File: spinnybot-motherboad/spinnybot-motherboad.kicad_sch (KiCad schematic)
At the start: 52 parts, among them J1 LEDSTRIP1_CONN, J10 M2_GND, J11 M3_12V, J12 M3_GND, J13 GND, J14 M2_12V, J15 M3_SERIAL_CONN, J16 M2_SERIAL_CONN, J17 M1_SERIAL_CONN, J2 LEDSTRIP2_CONN, J3 LEDSTRIP3_CONN, J4 XBEE RESET, J5 XBEE FTDI, J6 CAP SWITCH, J7 +12V, J8 M1_12V, J9 M1_GND, Q1 SISA96DN, U1 SN74AHCT541N, U2 LM1117-5.0, U3 LM1117-3.3, U4 SN74LVC1G74, U5 XBP9B-DMWT-002

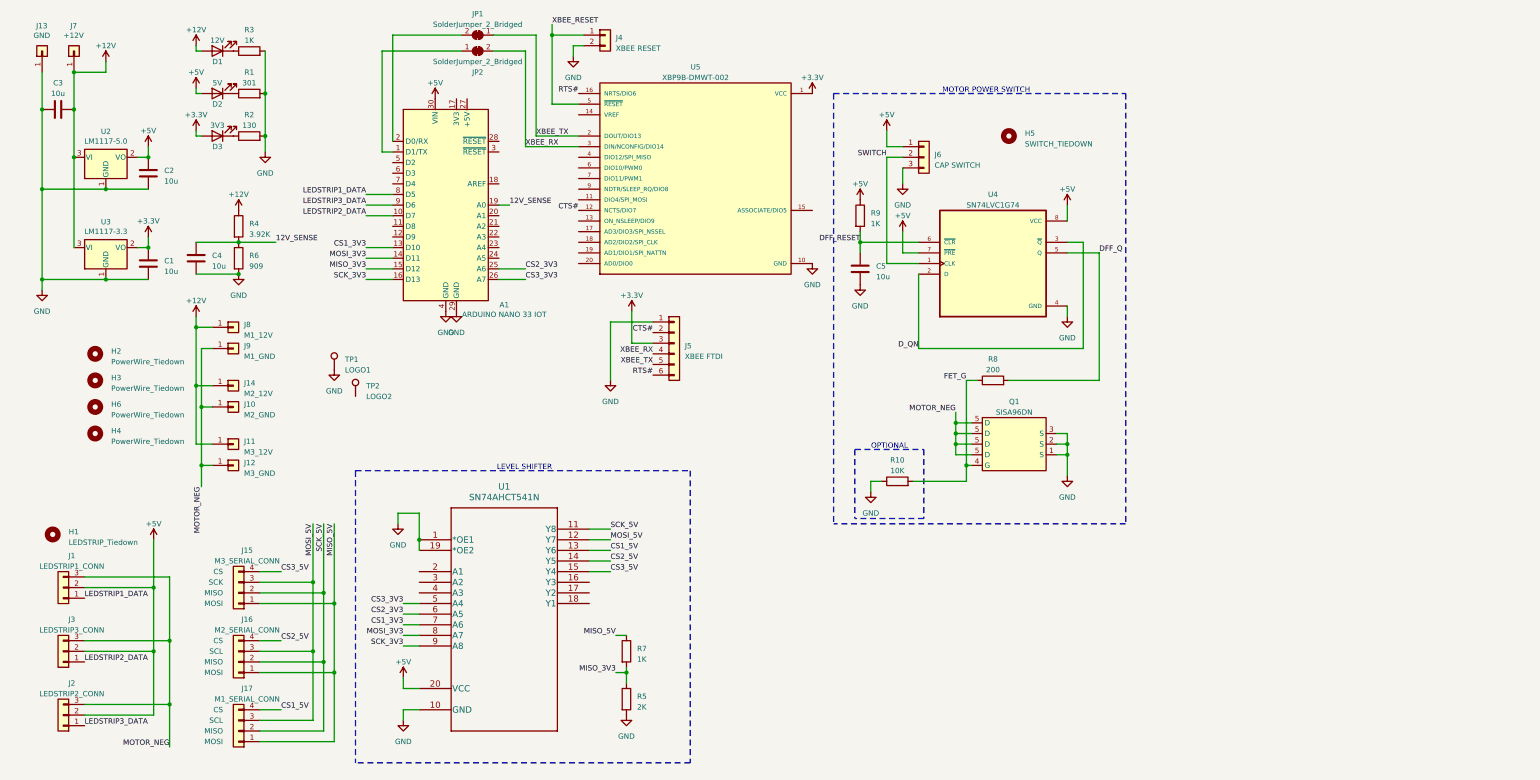
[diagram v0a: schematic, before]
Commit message: board rev 2, got all components placed. still need to route
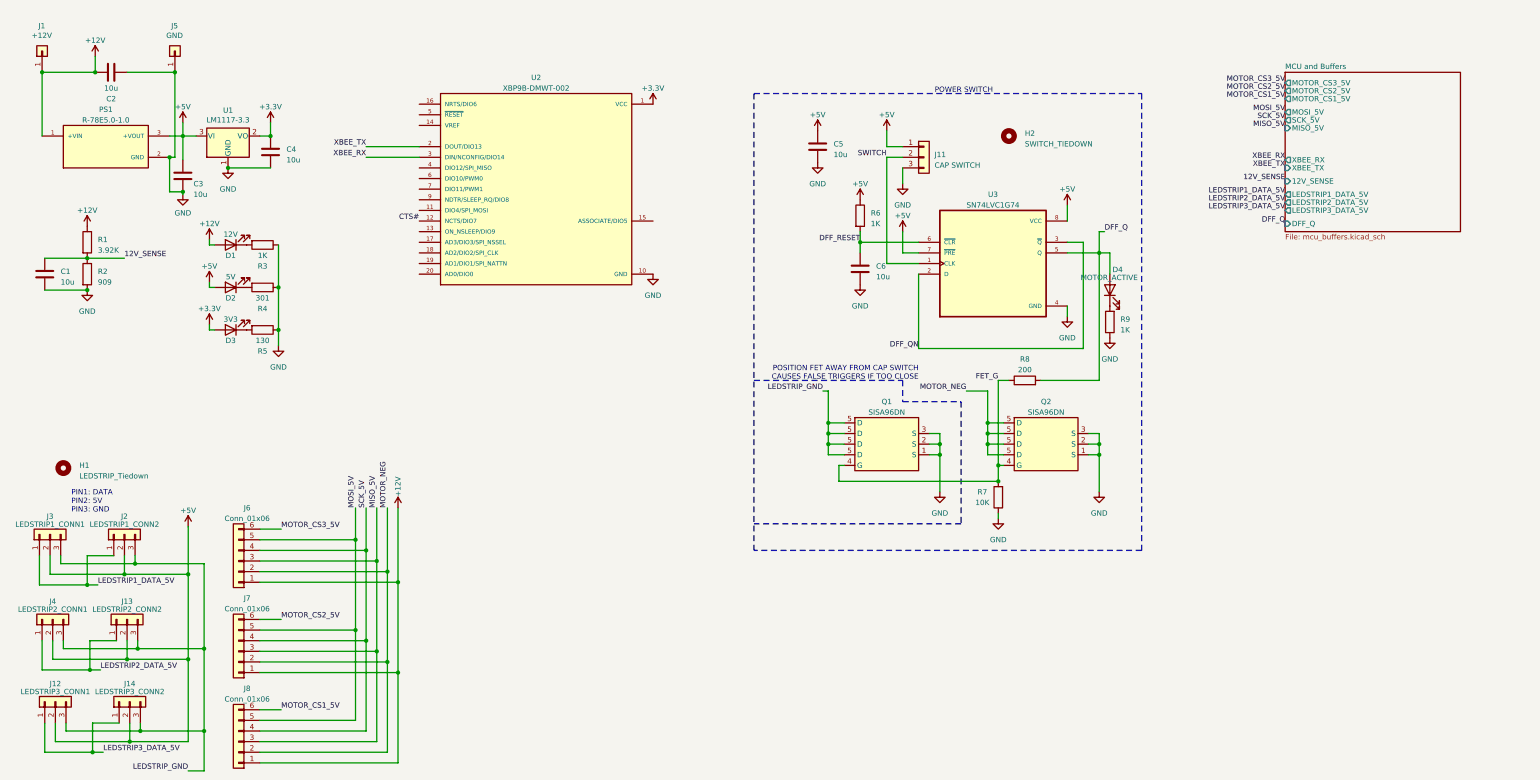
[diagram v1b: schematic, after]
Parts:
- removed A1: ARDUINO NANO 33 IOT, Module:Arduino_Nano, symbol MCU_Module:Arduino_Nano_v3.x
- removed C1, C2: 10u, Capacitor_SMD:C_1206_3216Metric_Pad1.33x1.80mm_HandSolder, symbol Device:C
- removed H2, H3, H4, H6: PowerWire_Tiedown, MountingHole:MountingHole_3mm, symbol Mechanical:MountingHole
- removed J10: M2_GND, TestPoint:TestPoint_Pad_2.5x2.5mm, symbol Connector_Generic:Conn_01x01
- removed J11: M3_12V, TestPoint:TestPoint_Pad_2.5x2.5mm, symbol Connector_Generic:Conn_01x01
- removed J12: M3_GND, TestPoint:TestPoint_Pad_2.5x2.5mm, symbol Connector_Generic:Conn_01x01
- removed J14: M2_12V, TestPoint:TestPoint_Pad_2.5x2.5mm, symbol Connector_Generic:Conn_01x01
- removed J15: M3_SERIAL_CONN, Connector_PinHeader_2.54mm:PinHeader_1x04_P2.54mm_Vertical, symbol spinnybot:motor_serial_connector
- removed J16: M2_SERIAL_CONN, Connector_PinHeader_2.54mm:PinHeader_1x04_P2.54mm_Vertical, symbol spinnybot:motor_serial_connector
- removed J17: M1_SERIAL_CONN, Connector_PinHeader_2.54mm:PinHeader_1x04_P2.54mm_Vertical, symbol spinnybot:motor_serial_connector
- removed J2: LEDSTRIP2_CONN, Connector_PinHeader_2.54mm:PinHeader_1x03_P2.54mm_Vertical, symbol Connector_Generic:Conn_01x03
- removed J4: XBEE RESET, Connector_PinHeader_2.54mm:PinHeader_1x02_P2.54mm_Vertical, symbol Connector_Generic:Conn_01x02
- removed J5: XBEE FTDI, Connector_PinHeader_2.54mm:PinHeader_1x06_P2.54mm_Vertical, symbol Connector_Generic:Conn_01x06
- removed J8: M1_12V, TestPoint:TestPoint_Pad_2.5x2.5mm, symbol Connector_Generic:Conn_01x01
- removed J9: M1_GND, TestPoint:TestPoint_Pad_2.5x2.5mm, symbol Connector_Generic:Conn_01x01
- removed JP1, JP2: SolderJumper_2_Bridged, Jumper:SolderJumper-2_P1.3mm_Open_RoundedPad1.0x1.5mm, symbol Jumper:SolderJumper_2_Bridged
- removed R5: 2K, Resistor_SMD:R_0805_2012Metric_Pad1.20x1.40mm_HandSolder, symbol Device:R
- removed R7: 1K, Resistor_SMD:R_0805_2012Metric_Pad1.20x1.40mm_HandSolder, symbol Device:R
- removed TP1: LOGO1, robologo-shenzen:F.Mask_g1609, symbol Connector:TestPoint
- removed TP2: LOGO2, robologo-shenzen:F.SilkS_g1611, symbol Connector:TestPoint
- removed U1: SN74AHCT541N, SN74AHCT541N:SN74AHCT541N, symbol SN74AHCT541N:SN74AHCT541N
- removed U2: LM1117-5.0, Package_TO_SOT_SMD:SOT-223-3_TabPin2, symbol Regulator_Linear:LM1117-5.0
- removed U3: LM1117-3.3, Package_TO_SOT_SMD:SOT-223-3_TabPin2, symbol Regulator_Linear:LM1117-3.3
- added C3, C4, C5: 10u, Capacitor_SMD:C_1206_3216Metric_Pad1.33x1.80mm_HandSolder, symbol Device:C
- added D4: MOTOR_ACTIVE, LED_SMD:LED_0805_2012Metric_Pad1.15x1.40mm_HandSolder, symbol Device:LED
- added J12: LEDSTRIP3_CONN1, B3B-PH-SM4:JST_B3B-PH-SM4-TB(LF)(SN), symbol Connector_Generic:Conn_01x03
- added J13: LEDSTRIP2_CONN2, B3B-PH-SM4:JST_B3B-PH-SM4-TB(LF)(SN), symbol Connector_Generic:Conn_01x03
- added J14: LEDSTRIP3_CONN2, B3B-PH-SM4:JST_B3B-PH-SM4-TB(LF)(SN), symbol Connector_Generic:Conn_01x03
- added J4: LEDSTRIP2_CONN1, B3B-PH-SM4:JST_B3B-PH-SM4-TB(LF)(SN), symbol Connector_Generic:Conn_01x03
- added J6, J7, J8: Conn_01x06, S6B-XH-SM4-TB:S6B-XH-SM4-TBLFSN, symbol Connector_Generic:Conn_01x06
- added PS1: R-78E5.0-1.0, R-78E5:CONV_R-78E5.0-1.0, symbol R-78E5.0-1.0:R-78E5.0-1.0
- added Q1: SISA96DN, Package_SO:Vishay_PowerPAK_1212-8_Single, symbol spinnybot:SISA96DN
- added R9: 1K, Resistor_SMD:R_0805_2012Metric_Pad1.20x1.40mm_HandSolder, symbol Device:R
- added U1: LM1117-3.3, Package_TO_SOT_SMD:SOT-223-3_TabPin2, symbol Regulator_Linear:LM1117-3.3
- J2: renamed from J1; value LEDSTRIP1_CONN -> LEDSTRIP1_CONN2; footprint Connector_PinHeader_2.54mm:PinHeader_1x03_P2.54mm_Vertical -> B3B-PH-SM4:JST_B3B-PH-SM4-TB(LF)(SN)
- J3: value LEDSTRIP3_CONN -> LEDSTRIP1_CONN1; footprint Connector_PinHeader_2.54mm:PinHeader_1x03_P2.54mm_Vertical -> B3B-PH-SM4:JST_B3B-PH-SM4-TB(LF)(SN)
- renumbered C4 to C1, C3 to C2, C5 to C6, H5 to H2, J7 to J1, J6 to J11, J13 to J5, Q1 to Q2, R4 to R1, R6 to R2, R1 to R4, R2 to R5, R9 to R6, R10 to R7, U5 to U2, U4 to U3
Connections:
- net LEDSTRIP2_DATA is gone; now on net LEDSTRIP1_DATA_5V: J3.1 (Pin_1)
- net +12V: now also J6.1 (Pin_1), J7.1 (Pin_1), J8.1 (Pin_1), PS1.1 (+VIN)
- net +3V3: now also C4.1, U1.2 (VO)
- net +5V: now also C3.1, C5.1, J12.2 (Pin_2), J13.2 (Pin_2), J14.2 (Pin_2), J4.2 (Pin_2), PS1.3 (+VOUT), U1.3 (VI)
- net DFF_Q: now also D4.2 (A)
- net FET_G: now also Q1.4 (G)
- net GND: now also R3.1, R4.1, R5.1, C3.2, C4.2, C5.2, PS1.2 (GND), Q1.1 (S), Q1.2 (S), Q1.3 (S), R9.1, U1.1 (GND); no longer R3.2, R4.2, R5.2
- net MISO_5V: now also J6.3 (Pin_3), J7.3 (Pin_3), J8.3 (Pin_3)
- net MOSI_5V: now also J6.5 (Pin_5), J7.5 (Pin_5), J8.5 (Pin_5)
- net MOTOR_NEG: now also J6.2 (Pin_2), J7.2 (Pin_2), J8.2 (Pin_2); no longer J2.3 (Pin_3), J3.3 (Pin_3)
- net SCK_5V: now also J6.4 (Pin_4), J7.4 (Pin_4), J8.4 (Pin_4)
- net at D3.1 (K): now also R5.2; no longer R5.1
- net at D1.1 (K): now also R3.2; no longer R3.1
- net at D2.1 (K): now also R4.2; no longer R4.1
- net D_QN renamed DFF_QN
- net LEDSTRIP1_DATA renamed LEDSTRIP1_DATA_5V
- net RTS#: no longer names the net of U2.16 (NRTS/DIO6)
- net XBEE_RESET: no longer names the net of U2.5 (~RESET)
- new net: D4.1 (K), R9.2
- new net LEDSTRIP2_DATA_5V: J13.1 (Pin_1), J4.1 (Pin_1)
- new net LEDSTRIP3_DATA_5V: J12.1 (Pin_1), J14.1 (Pin_1)
- new net LEDSTRIP_GND: J12.3 (Pin_3), J13.3 (Pin_3), J14.3 (Pin_3), J2.3 (Pin_3), J3.3 (Pin_3), J4.3 (Pin_3), Q1.5 (D)
- new net MOTOR_CS1_5V: J8.6 (Pin_6)
- new net MOTOR_CS2_5V: J7.6 (Pin_6)
- new net MOTOR_CS3_5V: J6.6 (Pin_6)
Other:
- added sheet MCU and Buffers (mcu_buffers.kicad_sch)
- note added: "PIN1: DATA PIN2: 5V PIN3: GND"
- note added: "POSITION FET AWAY FROM CAP SWITCH CAUSES FALSE TRIGGERS IF TOO CLOSE"
- note added: "POWER SWITCH"
- note removed: "LEVEL SHIFTER"
- note removed: "MOTOR POWER SWITCH"
- note removed: "OPTIONAL"
- moved on the sheet: C1, C2, D1, D2, D3, H1, J1, J2, J5, Q2, R1, R2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

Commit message: routed rev2 mainboard
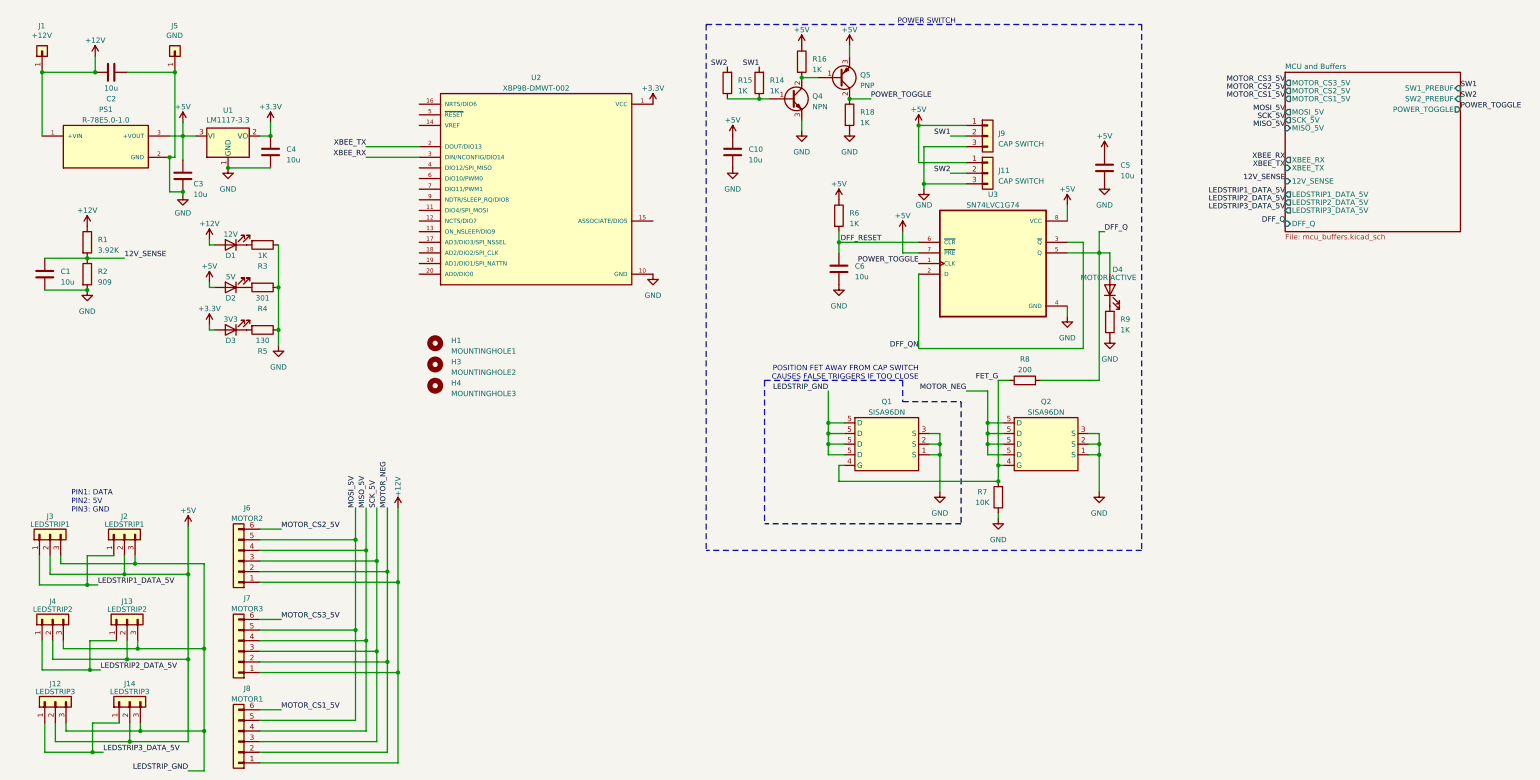
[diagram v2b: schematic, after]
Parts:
- removed H2: SWITCH_TIEDOWN, MountingHole:MountingHole_3mm, symbol Mechanical:MountingHole
- added C10: 10u, Capacitor_SMD:C_1206_3216Metric_Pad1.33x1.80mm_HandSolder, symbol Device:C
- added H3: MOUNTINGHOLE2, custom:MountingHole_3.3mm, symbol Mechanical:MountingHole
- added H4: MOUNTINGHOLE3, custom:MountingHole_3.3mm, symbol Mechanical:MountingHole
- added J9: CAP SWITCH, B3B-PH-SM4:JST_B3B-PH-SM4-TB(LF)(SN), symbol Connector_Generic:Conn_01x03
- added Q4: NPN, Package_TO_SOT_THT:TO-92_Inline, symbol Device:Q_NPN_BCE
- added Q5: PNP, Package_TO_SOT_THT:TO-92_Inline, symbol Device:Q_PNP_BCE
- added R14, R15, R16, R18: 1K, Resistor_SMD:R_0805_2012Metric_Pad1.20x1.40mm_HandSolder, symbol Device:R
- D4: value MOTOR_ACTIVE -> MOTOR ACTIVE
- H1: value LEDSTRIP_Tiedown -> MOUNTINGHOLE1; footprint MountingHole:MountingHole_3mm -> custom:MountingHole_3.3mm
- J11: footprint Connector_PinHeader_2.54mm:PinHeader_1x03_P2.54mm_Vertical -> B3B-PH-SM4:JST_B3B-PH-SM4-TB(LF)(SN)
- J12: value LEDSTRIP3_CONN1 -> LEDSTRIP3
- J13: value LEDSTRIP2_CONN2 -> LEDSTRIP2
- J14: value LEDSTRIP3_CONN2 -> LEDSTRIP3
- J2: value LEDSTRIP1_CONN2 -> LEDSTRIP1
- J3: value LEDSTRIP1_CONN1 -> LEDSTRIP1
- J4: value LEDSTRIP2_CONN1 -> LEDSTRIP2
- J5: footprint Connector_Wire:SolderWirePad_1x01_SMD_5x10mm -> custom:Stitched_SolderWirePad_1x01_SMD_5x10mm
- J6: value Conn_01x06 -> MOTOR2
- J7: value Conn_01x06 -> MOTOR3
- J8: value Conn_01x06 -> MOTOR1
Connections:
- net +5V: now also C10.1, J9.1 (Pin_1), Q5.3 (E), R16.1
- net GND: now also C10.2, J9.3 (Pin_3), Q4.3 (E), R18.2
- net MISO_5V: now also J6.4 (Pin_4), J7.4 (Pin_4), J8.4 (Pin_4); no longer J6.3 (Pin_3), J7.3 (Pin_3), J8.3 (Pin_3)
- net MOTOR_CS2_5V: now also J6.6 (Pin_6); no longer J7.6 (Pin_6)
- net MOTOR_CS3_5V: now also J7.6 (Pin_6); no longer J6.6 (Pin_6)
- net SCK_5V: now also J6.3 (Pin_3), J7.3 (Pin_3), J8.3 (Pin_3); no longer J6.4 (Pin_4), J7.4 (Pin_4), J8.4 (Pin_4)
- net CTS#: no longer names the net of U2.12 (NCTS/DIO7)
- net SWITCH renamed POWER_TOGGLE
- net POWER_TOGGLE: now also Q5.2 (C), R18.1; no longer J11.2 (Pin_2)
- new net: Q4.1 (B), R14.1, R15.1
- new net: Q4.2 (C), Q5.1 (B), R16.2
- new net SW1: J9.2 (Pin_2), R14.2
- new net SW2: J11.2 (Pin_2), R15.2
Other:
- sheet MCU and Buffers ports: added POWER_TOGGLE, SW1_PREBUF, SW2_PREBUF; removed none
- moved on the sheet: C5, C6, J11, R6
